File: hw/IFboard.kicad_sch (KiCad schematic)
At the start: 83 parts, among them J1 USB_C_Receptacle_USB2.0_16P, J2 Conn_01x03_Socket, J3 Conn_ARM_SWD_TagConnect_TC203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, J4 Conn_01x03_Socket, J5 Conn_01x03_Socket, J6 Conn_01x03_Socket, J7 Conn_01x01_MountingPin, SW3 SW_Push, SW4 SW_Push, SW5 SW_Push, SW6 SW_Push, U1 AMS1117-3.3, U2 XC6206PxxxMR, U3 TCAN3413DR, U4 ST4E1240DT, U5 MAX232ESE+T, U6 STM32G0B1CBTx, U7 ER_OLEDM0.91_1x-I2C

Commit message: changed position of SMSs and added TVS diodes to RS485 and CAN
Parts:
- added D13, D14: PESD2CANFD24V-UX, PZL:TVS_PESD2CANFD24V-UX, symbol newLib:PESD2CANFD24V-UX
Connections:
- net GND: now also D13.3, D14.3
- net at L1.2, U4.6 (A): no longer JP1.1 (A)
- net at L1.1, U4.7 (B): no longer R25.2
- net at J4.1 (Pin_1), L1.3: now also JP1.1 (A), D14.1
- net at J4.2 (Pin_2), L1.4: now also R25.2, D14.2
- net at J6.1 (Pin_1), L2.3: now also R15.2, D13.1
- net at J6.2 (Pin_2), L2.4: now also R14.1, D13.2
- net at L2.1, U3.7 (CANH): no longer R14.1
- net at L2.2, U3.6 (CANL): no longer R15.2
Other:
- note added: "${PRJNAME} Elektronik & Technische Informatik HTL Graz-Gösting"
- note added: "filter CM"
- note removed: "EMC Lab Elektronik & Technische Informatik HTL Graz-Gösting"
- moved on the sheet: C1, C10, C11, C12, C13, C14, C17, C18, C19, C2, C20, C21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

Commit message: wip:testpoints
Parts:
- added TP1: TestPoint, PZL:TestPoint_Keystone_5019_Miniature, symbol Connector:TestPoint
- added TP2, TP3, TP4, TP5: TestPoint, TestPoint:TestPoint_Keystone_5005-5009_Compact, symbol Connector:TestPoint
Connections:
- net GND: now also TP1.1
- net at D14.1, J4.1 (Pin_1), JP1.1 (A)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: now also TP5.1
- net at D14.2, J4.2 (Pin_2), L1.4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: now also TP4.1
- net at D13.1, J6.1 (Pin_1), L2.3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: now also TP3.1
- net at D13.2, J6.2 (Pin_2), L2.4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: now also TP2.1

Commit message: wip:testpoints
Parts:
- added JP2: Jumper_2_Open, Connector_PinHeader_2.54mm:PinHeader_1x02_P2.54mm_Vertical, symbol Jumper:Jumper_2_Open
- added R26, R27: 1k, Resistor_SMD:R_0603_1608Metric, symbol Device:R
- added TP6, TP7, TP8, TP9: TestPoint, TestPoint:TestPoint_Keystone_5005-5009_Compact, symbol Connector:TestPoint
- C24: now not fitted
- U7: footprint Display:ER_OLEDM0.91_1x-I2C -> PZL:ER_OLEDM0.91_1x-I2C
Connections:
- net GND: now also R26.1, R27.1
- net USART4_RX_MAX: now also TP9.1
- net USART4_TX_MAX: now also TP8.1
- net at J2.2 (Pin_2), R8.1: now also TP7.1
- net at D13.2, J6.2 (Pin_2), L2.4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: now also JP2.1 (A); no longer R14.1
- net at J2.1 (Pin_1), R7.1: now also TP6.1
- net TODO_EN_CAN_TERM: now reaches U6.26 (PB14)
- net at U3.5 (SHDN): now also R26.2
- net at U3.8 (S): now also R27.2
- new net: JP2.2 (B), R14.1
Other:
- note added: "CAN is multidrop -> "one long line" with 120 Ohms termination at both cable ends -> terminate at the cable ends, not on the nodes OR take care for termination when a terminating node is removed -> keep stubs short (<30cm for 1Mbps), and do not terminate stubs DLW31SH222SQ2#"
- note added: "CAN: open collector: recessive state NOT driven"
- note added: "RS485: bothe levels (high and low) are driven"
- note added: "Receiver CM: +/-30V ±58-V bus fault protection"
- note added: "all-in-one transceiver: THVD4421"
- note added: "always on"
- note added: "match R14/15 within 1% to avoid CM->DM conversion 4.7nF with 2+60 Ohms -> fg(-3dB) ~1Mbps"
- note added: "shutdown = high -> CANH=CANL=high-Z to GND"
- note removed: "match R14/15 within 1% to avoid CM->DM conversion"
- moved on the sheet: D4, D5, J5, J7, R10, R11

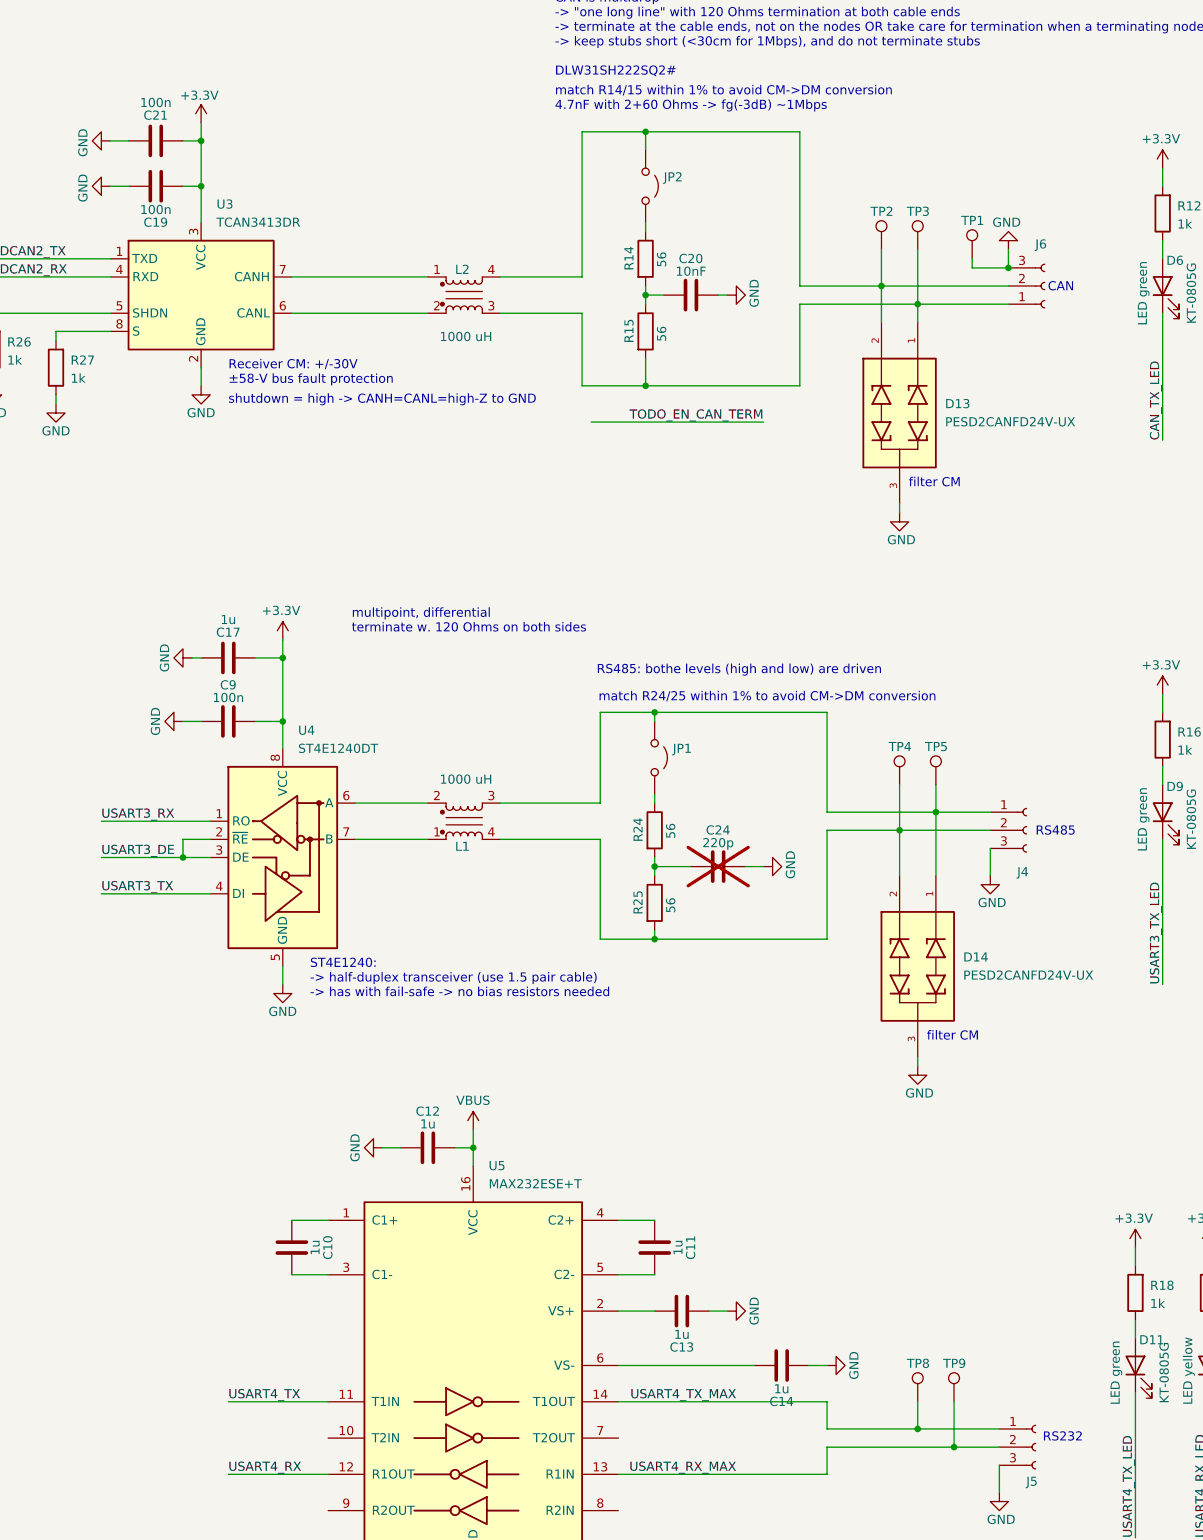
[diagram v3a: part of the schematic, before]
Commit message: added jumper to add/remove split-termination capacitors
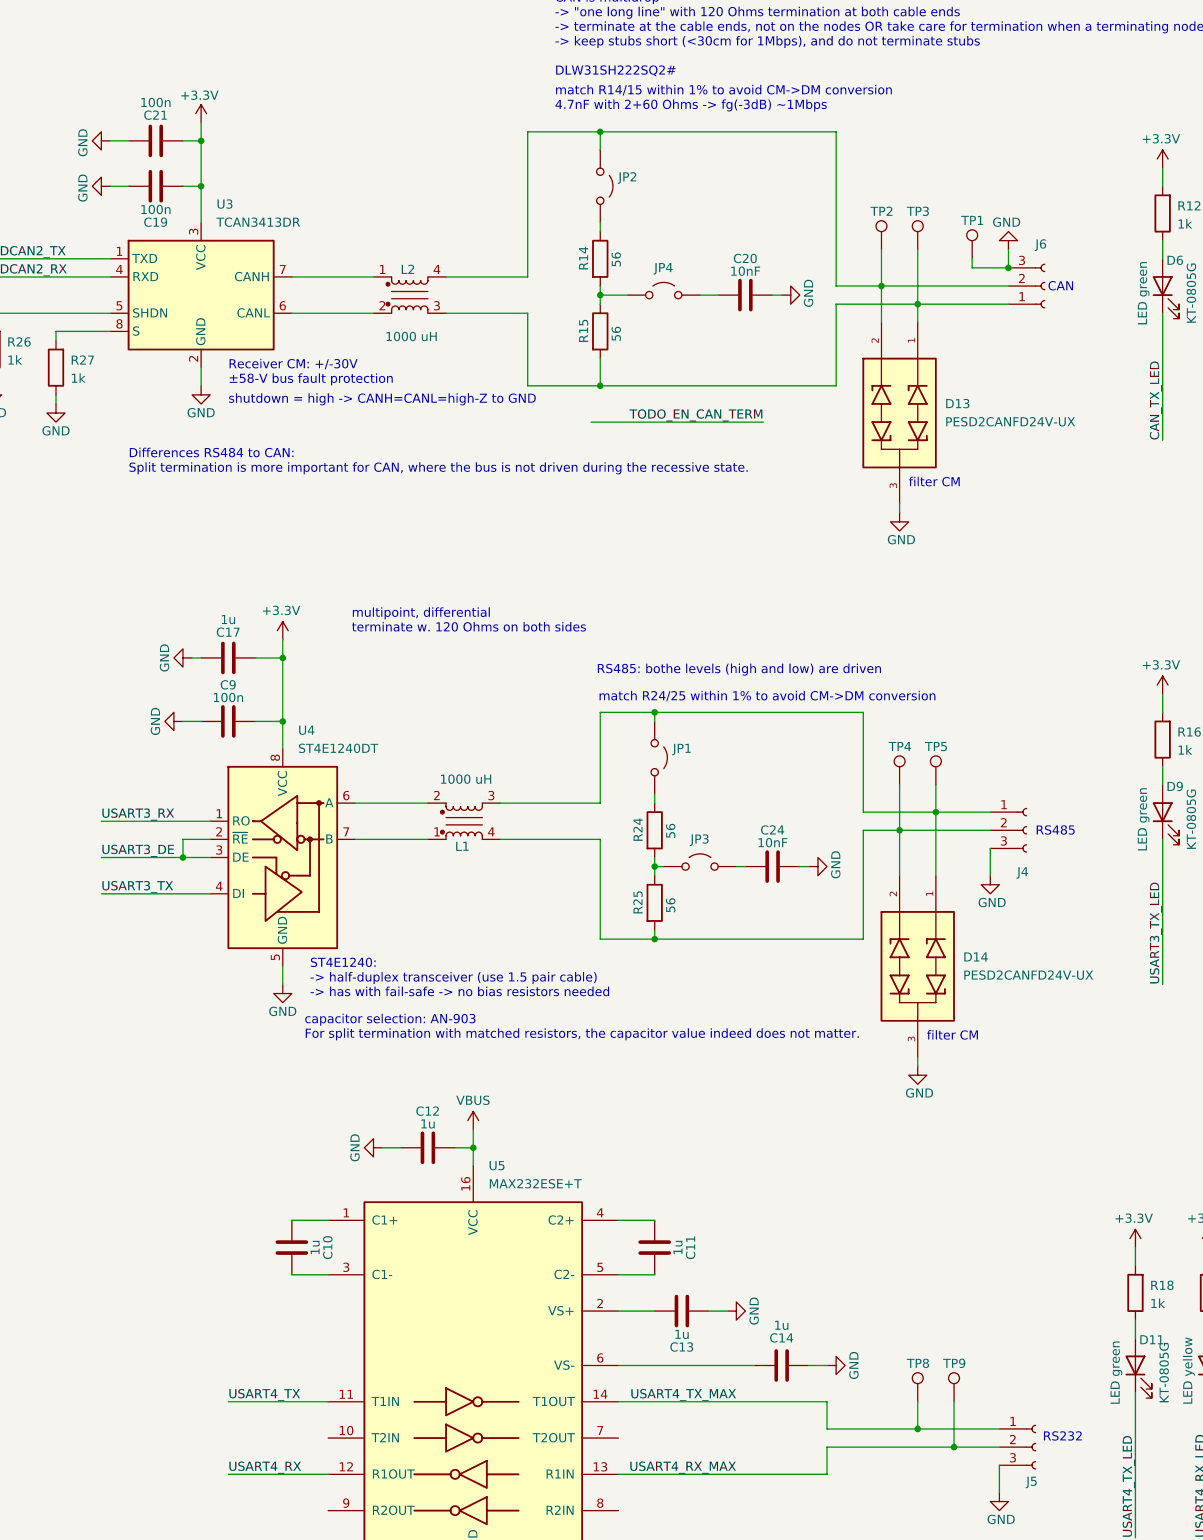
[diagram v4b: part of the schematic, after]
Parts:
- added JP3, JP4: Jumper_2_Open, Connector_PinHeader_2.54mm:PinHeader_1x02_P2.54mm_Vertical, symbol Jumper:Jumper_2_Open
- C24: value 220p -> 10nF; LCSC Part # C1530 -> C15195; now fitted
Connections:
- net at R24.2, R25.1: now also JP3.1 (A); no longer C24.2
- net at R14.2, R15.1: now also JP4.1 (A); no longer C20.2
- new net: C24.2, JP3.2 (B)
- new net: C20.2, JP4.2 (B)
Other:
- note added: "Differences RS484 to CAN: Split termination is more important for CAN, where the bus is not driven during the recessive state."
- note added: "capacitor selection: AN-903 For split termination with matched resistors, the capacitor value indeed does not matter."
- moved on the sheet: C20, JP2, L2, R14, R15

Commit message: train session
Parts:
- added J10, J8, J9: Conn_01x01_MountingPin, Connector_PinHeader_1.00mm:PinHeader_1x01_P1.00mm_Vertical, symbol Connector_Generic_MountingPin:Conn_01x01_MountingPin
- added TP10, TP11: TestPoint, PZL:TestPoint_Keystone_5019_Miniature, symbol Connector:TestPoint
- R14, R15, R24, R25: value 56 -> 68; LCSC Part # C17757 -> C17802
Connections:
- net GND: now also TP10.1, TP11.1
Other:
- moved on the sheet: J4, J7

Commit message: cleanup
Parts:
- J10, J7, J8, J9: value Conn_01x01_MountingPin -> IcoTec_36650.2; footprint Connector_PinHeader_1.00mm:PinHeader_1x01_P1.00mm_Vertical -> PZ:icotek 36650.2 PCB-4-V-6,8SKL 3-6; symbol Connector_Generic_MountingPin:Conn_01x01_MountingPin -> PZ:IcoTec_36650.2
- U2: value XC6206PxxxMR -> XC6206P332MR-G; symbol Regulator_Linear:XC6206PxxxMR -> PZ:XC6206P332MR-G
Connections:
- net GND: now also J10.1 (MountPin), J7.1 (MountPin), J8.1 (MountPin), J9.1 (MountPin)
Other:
- note added: "J6 mates with FK-MC 0,5/ 3-ST-2,5 0,14 mm² ... 0,5 mm² (20-26AWG) Abisolierlänge: 8mm"
- note added: "Schirmdurchmesser: 3-6mm"
- note removed: "FK-MC 0,5/ 3-ST-2,5"
- note removed: "MC_1,5_3-G-3.5_1x03_P3.50mm"
- note removed: "XC6206P332MR-G"
- note removed: "mating (for 0,2-1,5 mm2) MC 1,5/3-ST-3,5 FMC 1,5/3-ST-3,5"
